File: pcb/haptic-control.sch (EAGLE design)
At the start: 131 parts, among them M1 SPH0641LM4H-1, P1 2P-PAD_1X3.5, P2 2P-PAD_1X3.5, P3 2P-PAD_1X3.5, P4 2P-PAD_1X3.5, U1 MIC23159, U10 DRV2605L, U11 DRV2605L, U12 MTCH6301, U2 BQ51050B, U3 FS312F-G, U4 FS8205, U5 CC2642R, U6 SST26VF064B, U7 74LVC1G17, U8 ICM20948, U9 PCA9306-DCU, X1 48MHz, X2 32.768kHz

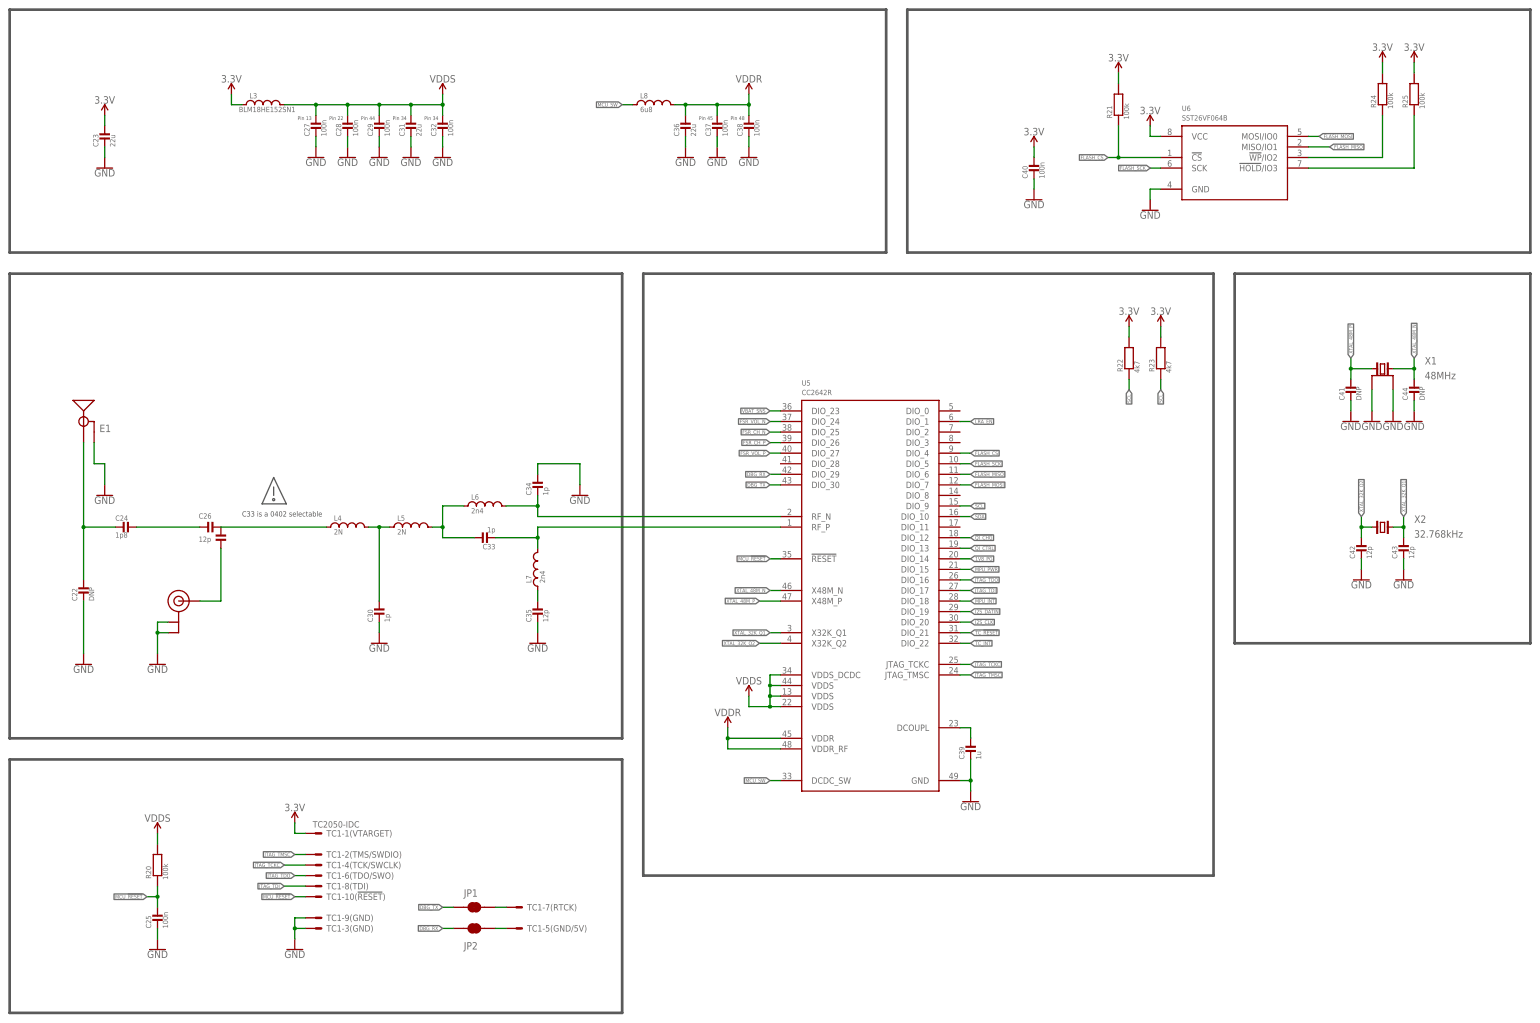
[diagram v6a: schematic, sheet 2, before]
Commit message: added notes to schematic
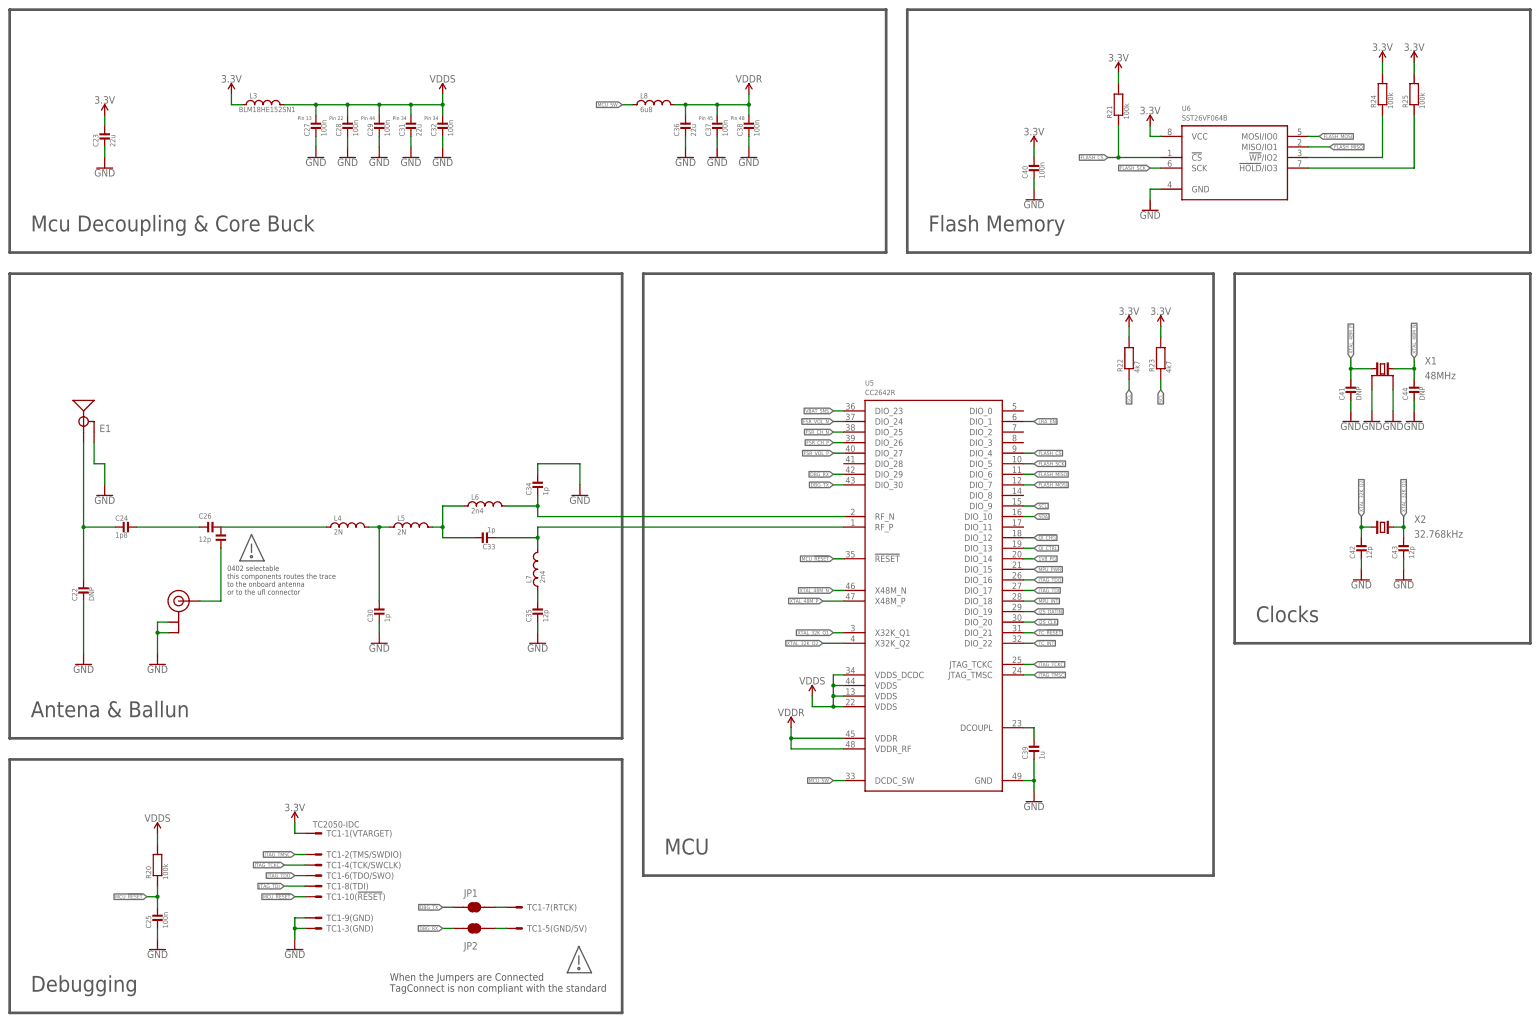
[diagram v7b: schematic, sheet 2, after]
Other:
- note added: "0402 selectable this components routes the trace to the onboard antenna or to the ufl connector"
- note added: "Antena & Ballun"
- note added: "Battery Protection Circuit"
- note added: "Clocks"
- note added: "Debugging"
- note added: "FSR Buttons"
- note added: "Flash Memory"
- note added: "Icharge = KIlim / RIlim RIlim = R1 + R2 KIlim = 314 Icharge = 234mA @ R1 = 1k2"
- note added: "LRA Haptic FB"
- note added: "MCU"
- note added: "MPU"
- note added: "Mcu Decoupling & Core Buck"
- note added: "Microphone"
- note added: "QI Charger"
- note added: "Supply Regulator"
- note added: "TODO: Verify Unpowered VREF1 Behaviour"
- note added: "Touch Controller"
- note added: "Vout = 1.43V @ 1kg"
- note added: "When the Jumpers are Connected TagConnect is non compliant with the standard"
- note removed: "C33 is a 0402 selectable"
- note removed: "Icharge = KIlim / RIlim RIlim = R11 + R12 KIlim = 314"
- moved on the sheet: C39, U5

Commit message: minor component placement and silkscreen changes
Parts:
- L1, L2, L8: device Passive Components > Inductors, Chokes & Coils:INDUCTOR_NC_0805 -> Passive Components > Inductors, Chokes & Coils:INDUCTOR_NC_0806
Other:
- note added: "When the Jumpers are Connected TagConnect is non compliant with the standard The jumpers connect a debug uart to unused pins on TagConnect"
- note removed: "When the Jumpers are Connected TagConnect is non compliant with the standard"
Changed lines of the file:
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@@
 <part name="C29" library="Passive Components &gt; Capacitors &gt; Multilayer Ceramic Capacitors MLCC" deviceset="MLCC" device="_0402" value="100n"/>
 <part name="C32" library="Passive Components &gt; Capacitors &gt; Multilayer Ceramic Capacitors MLCC" deviceset="MLCC" device="_0402" value="100n"/>
-<part name="L8" library="Passive Components &gt; Inductors, Chokes &amp; Coils" deviceset="INDUCTOR_NC" device="_0805" value="6u8"/>
+<part name="L8" library="Passive Components &gt; Inductors, Chokes &amp; Coils" deviceset="INDUCTOR_NC" device="_0806" value="6u8"/>
 <part name="L3" library="Passive Components &gt; Inductors, Chokes &amp; Coils" deviceset="INDUCTOR_NC" device="_0603" value="BLM18HE152SN1"/>
 <part name="C31" library="Passive Components &gt; Capacitors &gt; Multilayer Ceramic Capacitors MLCC" deviceset="MLCC" device="0603" value="22u"/>
@@
 <part name="P2" library="Connectors &gt; Other" deviceset="2P-PAD" device="_1X3.5"/>
 <part name="P1" library="Connectors &gt; Other" deviceset="2P-PAD" device="_1X3.5"/>
-<part name="L1" library="Passive Components &gt; Inductors, Chokes &amp; Coils" deviceset="INDUCTOR_NC" device="_0805" value="1u"/>
+<part name="L1" library="Passive Components &gt; Inductors, Chokes &amp; Coils" deviceset="INDUCTOR_NC" device="_0806" value="1u"/>
 <part name="C2" library="Passive Components &gt; Capacitors &gt; Multilayer Ceramic Capacitors MLCC" deviceset="MLCC" device="0603" value="4u7"/>
 <part name="C1" library="Passive Components &gt; Capacitors &gt; Multilayer Ceramic Capacitors MLCC" deviceset="MLCC" device="0603" value="1u"/>
@@
 <part name="GND4" library="Utility &gt; Power Symbols" deviceset="GND" device=""/>
 <part name="GND8" library="Utility &gt; Power Symbols" deviceset="GND" device=""/>
-<part name="L2" library="Passive Components &gt; Inductors, Chokes &amp; Coils" deviceset="INDUCTOR_NC" device="_0805" value="1u"/>
+<part name="L2" library="Passive Components &gt; Inductors, Chokes &amp; Coils" deviceset="INDUCTOR_NC" device="_0806" value="1u"/>
 <part name="C15" library="Passive Components &gt; Capacitors &gt; Multilayer Ceramic Capacitors MLCC" deviceset="MLCC" device="0603" value="4u7"/>
 <part name="C16" library="Passive Components &gt; Capacitors &gt; Multilayer Ceramic Capacitors MLCC" deviceset="MLCC" device="0603" value="1u"/>
@@
 <text x="12.7" y="76.2" size="3.81" layer="97">Antena &amp; Ballun</text>
 <text x="12.7" y="10.16" size="3.81" layer="97">Debugging</text>
-<text x="99.06" y="10.16" size="1.778" layer="97">When the Jumpers are Connected
-TagConnect is non compliant with the standard</text>
+<text x="82.296" y="8.128" size="1.778" layer="97">When the Jumpers are Connected
+TagConnect is non compliant with the standard
+The jumpers connect a debug uart to unused pins on TagConnect</text>
 <wire x1="144.526" y1="21.082" x2="141.732" y2="14.732" width="0.1524" layer="97"/>
 <wire x1="141.732" y1="14.732" x2="147.574" y2="14.732" width="0.1524" layer="97"/>
